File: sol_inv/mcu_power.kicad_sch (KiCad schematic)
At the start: 16 parts, among them SW1 SW_Push_Dual, U9 PSC3M5_E-LQFP-64

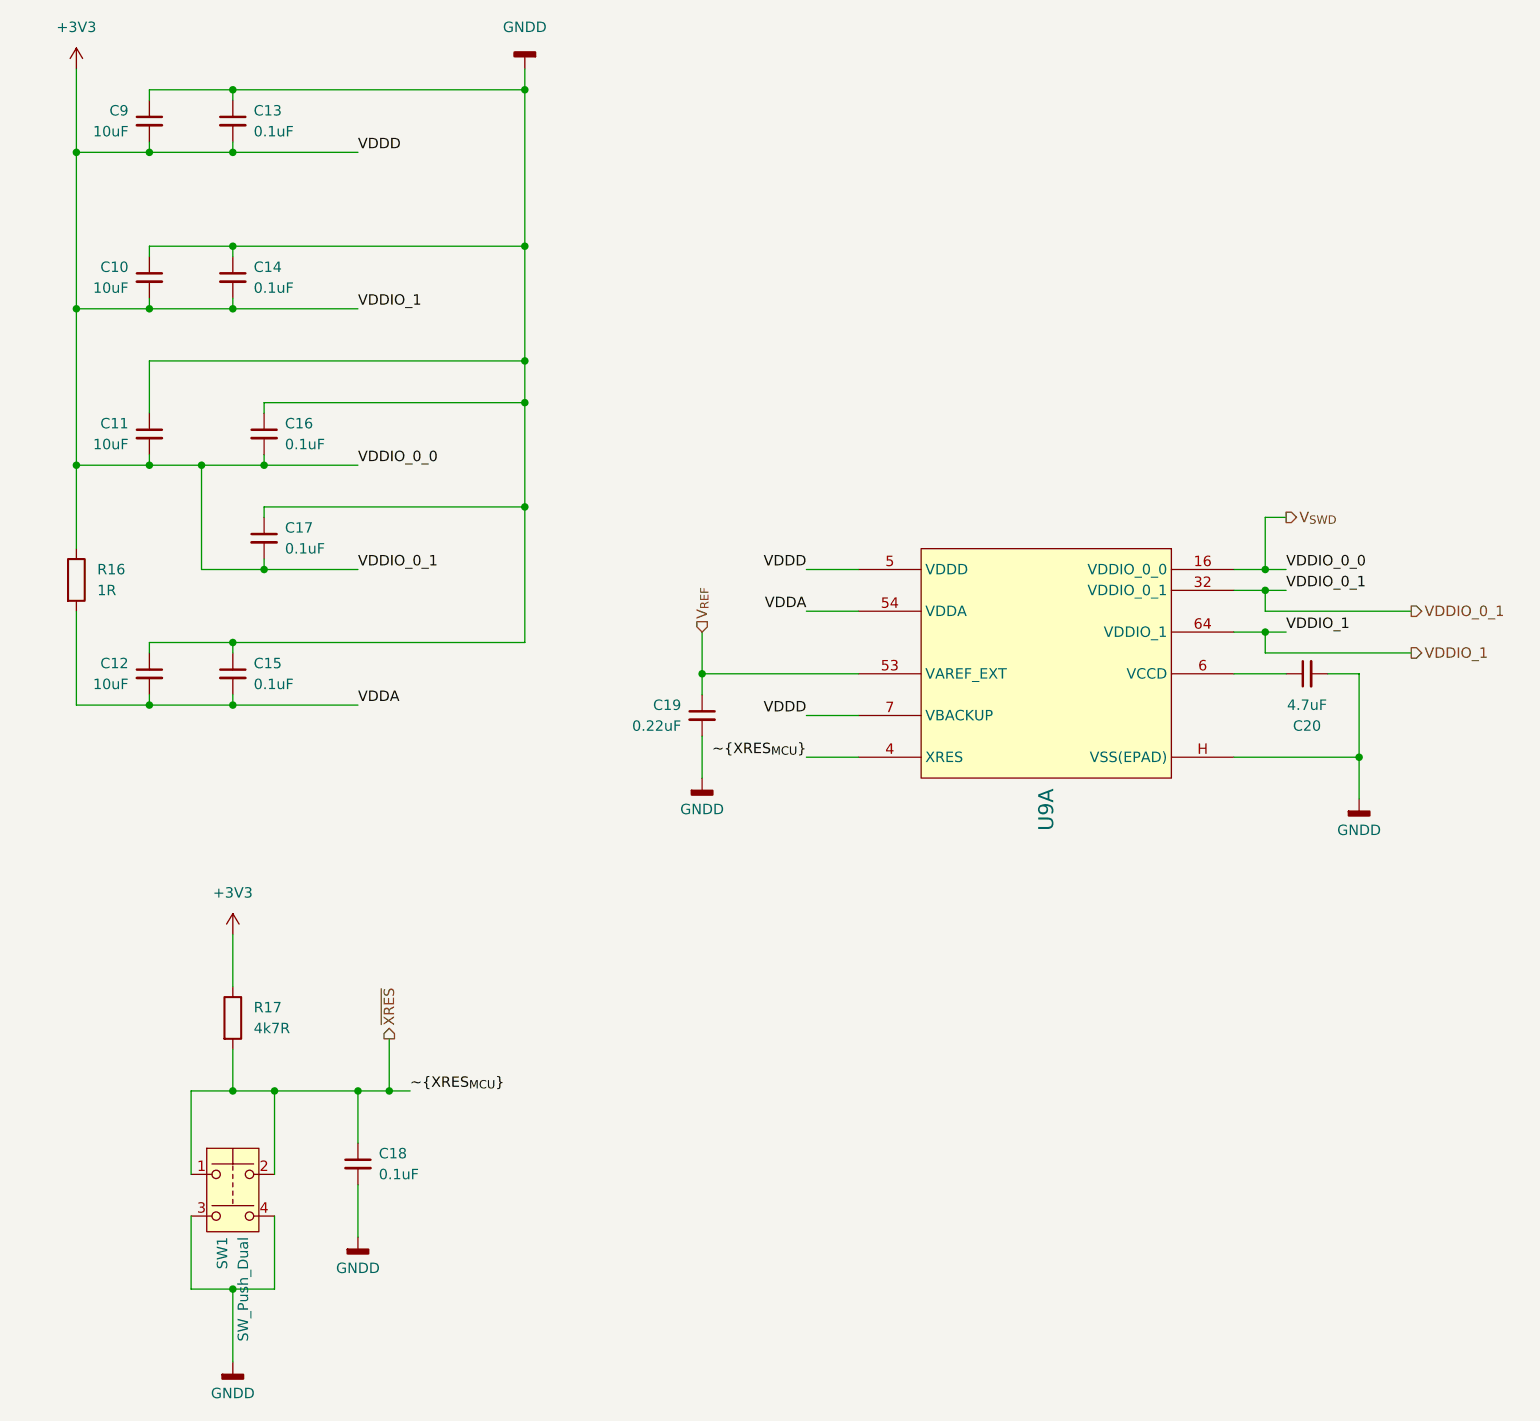
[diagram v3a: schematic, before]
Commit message: v0.3.4 fixes + component change for farnell
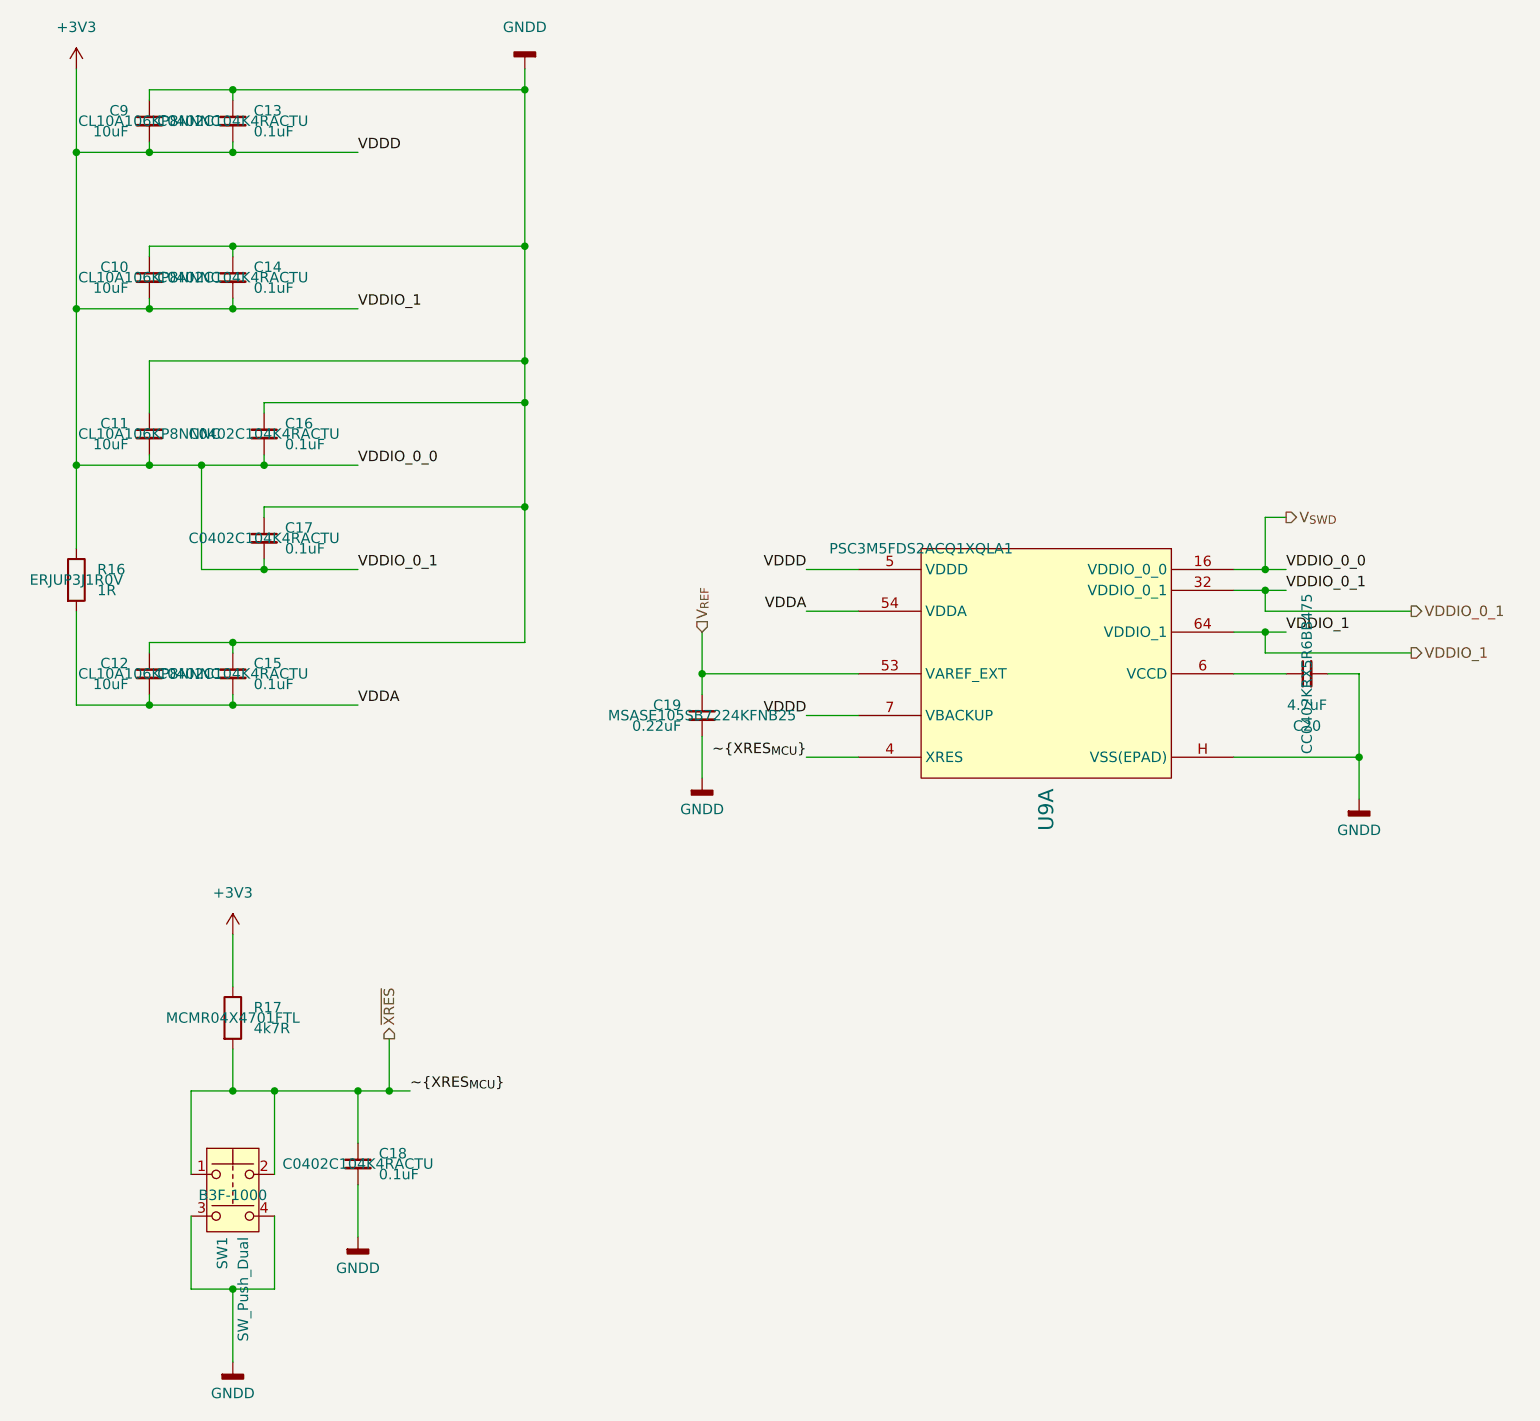
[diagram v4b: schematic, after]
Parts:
- C10, C11, C12, C9: Manufacturer Part Number (none) -> CL10A106KP8NNNC
- C13, C14, C15, C16, C17, C18: Manufacturer Part Number (none) -> C0402C104K4RACTU
- C19: Manufacturer Part Number (none) -> MSASE105SB7224KFNB25
- C20: Manufacturer Part Number (none) -> CC0402KRX5R6BB475
- R16: Manufacturer Part Number (none) -> ERJUP3J1R0V
- R17: Manufacturer Part Number (none) -> MCMR04X4701FTL
- SW1: Manufacturer Part Number (none) -> B3F-1000
- U9: Manufacturer Part Number (none) -> PSC3M5FDS2ACQ1XQLA1
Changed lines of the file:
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@@
+			)
+		)
+		(property "Manufacturer Part Number" "CC0402KRX5R6BB475"
+			(at 171.45 99.06 0)
+			(effects
+				(font
+					(size 1.27 1.27)
+				)
 			)
 		)
@@
 				)
 				(hide yes)
+			)
+		)
+		(property "Manufacturer Part Number" " B3F-1000"
+			(at 40.64 162.56 0)
+			(effects
+				(font
+					(size 1.27 1.27)
+				)
 			)
 		)
@@
 			)
 		)
+		(property "Manufacturer Part Number" "C0402C104K4RACTU"
+			(at 44.45 69.85 0)
+			(effects
+				(font
+					(size 1.27 1.27)
+				)
+			)
+		)
 		(pin "2"
 		)
@@
 			)
 		)
+		(property "Manufacturer Part Number" "MCMR04X4701FTL"
+			(at 40.64 140.97 0)
+			(effects
+				(font
+					(size 1.27 1.27)
+				)
+			)
+		)
 		(pin "2"
 		)
@@
 				)
 				(hide yes)
+			)
+		)
+		(property "Manufacturer Part Number" "MSASE105SB7224KFNB25"
+			(at 97.79 104.14 0)
+			(effects
+				(font
+					(size 1.27 1.27)
+				)
 			)
 		)
@@
 			)
 		)
+		(property "Manufacturer Part Number" "C0402C104K4RACTU"
+			(at 55.88 158.75 0)
+			(effects
+				(font
+					(size 1.27 1.27)
+				)
+			)
+		)
 		(pin "1"
 		)
@@
 				)
 				(hide yes)
+			)
+		)
+		(property "Manufacturer Part Number" "CL10A106KP8NNNC"
+			(at 30.48 69.85 0)
+			(effects
+				(font
+					(size 1.27 1.27)
+				)
 			)
 		)
@@
 			)
 		)
+		(property "Manufacturer Part Number" "C0402C104K4RACTU"
+			(at 40.64 31.75 0)
+			(effects
+				(font
+					(size 1.27 1.27)
+				)
+			)
+		)
 		(pin "2"
 		)
@@
 			)
 		)
+		(property "Manufacturer Part Number" "CL10A106KP8NNNC"
+			(at 30.48 99.06 0)
+			(effects
+				(font
+					(size 1.27 1.27)
+				)
+			)
+		)
 		(pin "2"
 		)
@@
 			)
 		)
+		(property "Manufacturer Part Number" "PSC3M5FDS2ACQ1XQLA1"
+			(at 124.46 83.82 0)
+			(effects
+				(font
+					(size 1.27 1.27)
+				)
+			)
+		)
 		(pin "58"
 		)
@@
 			)
 		)
+		(property "Manufacturer Part Number" "CL10A106KP8NNNC"
+			(at 30.48 50.8 0)
+			(effects
+				(font
+					(size 1.27 1.27)
+				)
+			)
+		)
 		(pin "2"
 		)
@@
 			)
 		)
+		(property "Manufacturer Part Number" "ERJUP3J1R0V"
+			(at 21.59 87.63 0)
+			(effects
+				(font
+					(size 1.27 1.27)
+				)
+			)
+		)
 		(pin "2"
 		)
@@
 			)
 		)
+		(property "Manufacturer Part Number" "C0402C104K4RACTU"
+			(at 40.64 99.06 0)
+			(effects
+				(font
+					(size 1.27 1.27)
+				)
+			)
+		)
 		(pin "2"
 		)
@@
 			)
 		)
+		(property "Manufacturer Part Number" "C0402C104K4RACTU"
+			(at 44.45 82.55 0)
+			(effects
+				(font
+					(size 1.27 1.27)
+				)
+			)
+		)
 		(pin "2"
 		)
@@
 				)
 				(hide yes)
+			)
+		)
+		(property "Manufacturer Part Number" "CL10A106KP8NNNC"
+			(at 30.48 31.75 0)
+			(effects
+				(font
+					(size 1.27 1.27)
+				)
 			)
 		)
@@
 			)
 		)
+		(property "Manufacturer Part Number" "C0402C104K4RACTU"
+			(at 40.64 50.8 0)
+			(effects
+				(font
+					(size 1.27 1.27)
+				)
+			)
+		)

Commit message: v0.4 fixed mcu ldo part, production testing
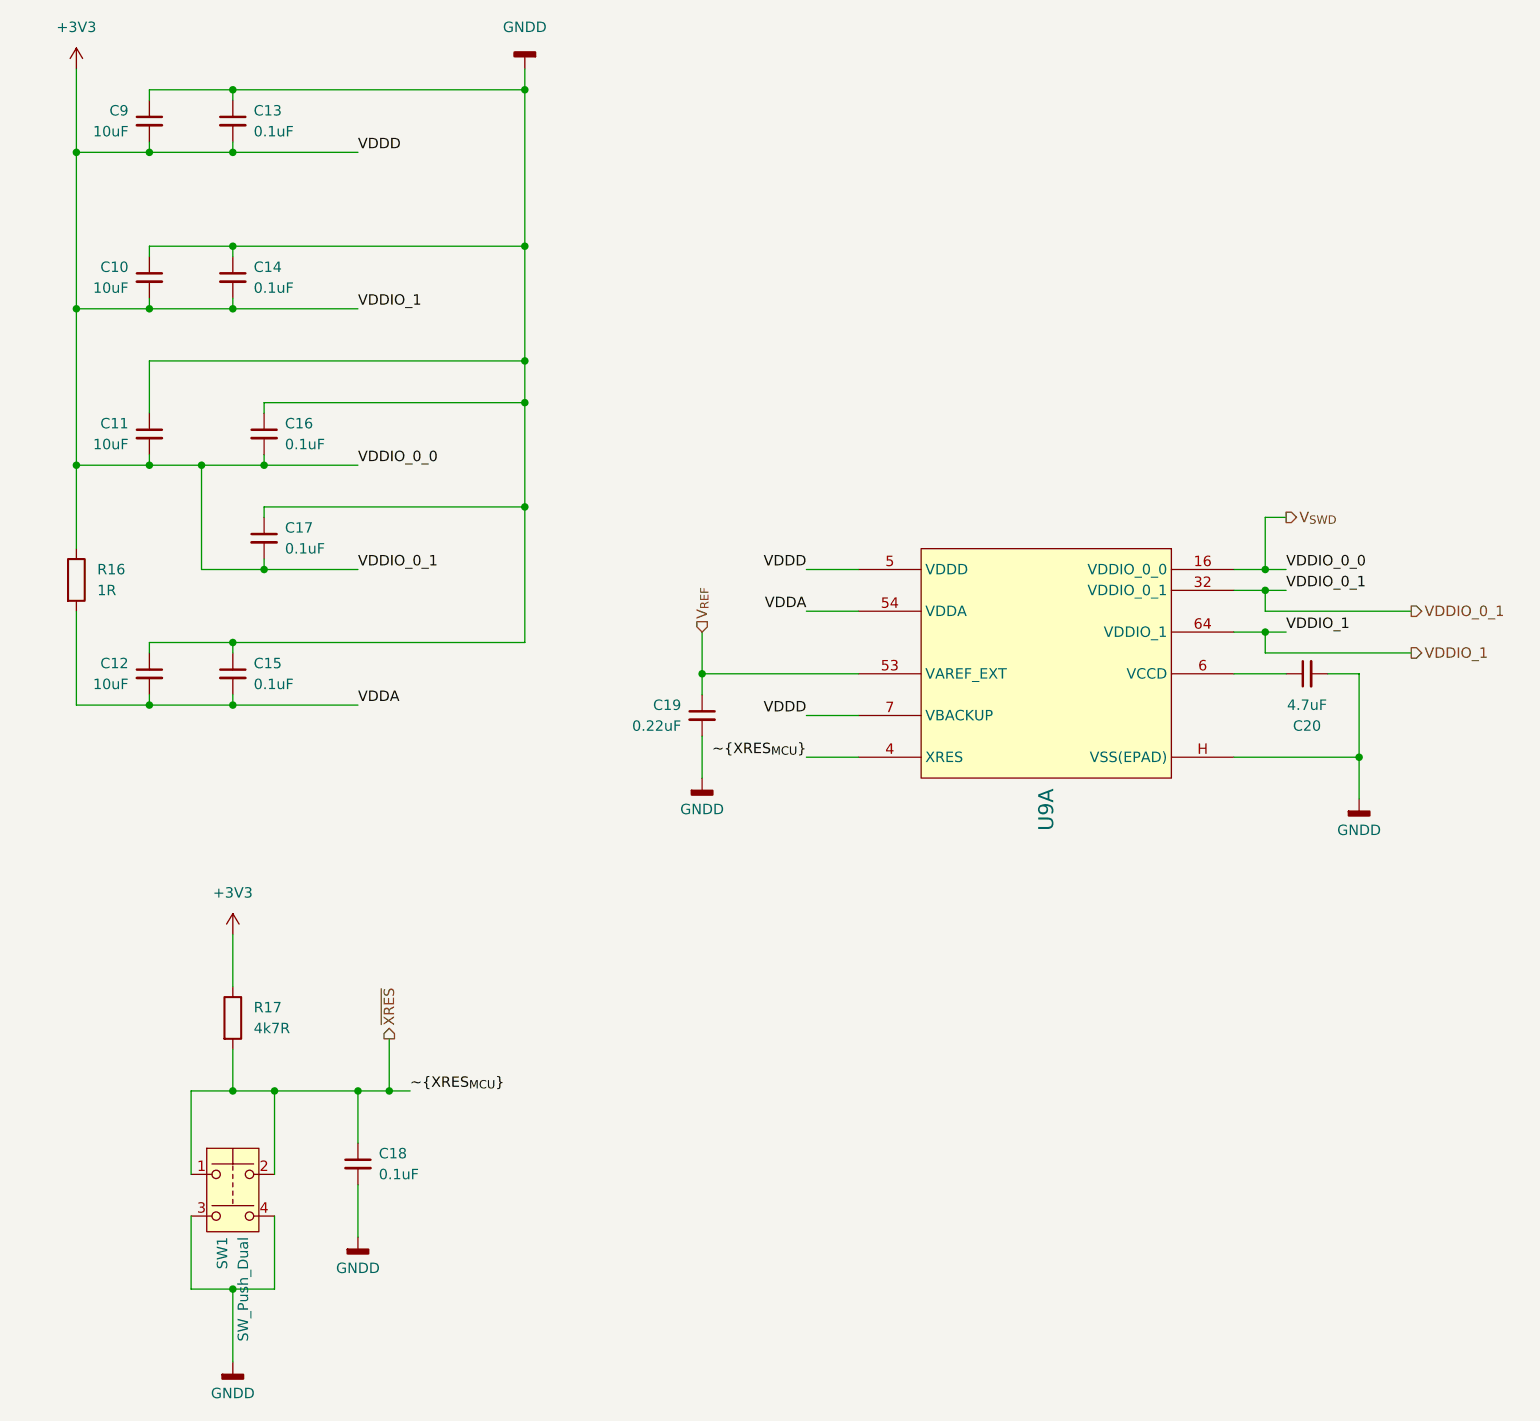
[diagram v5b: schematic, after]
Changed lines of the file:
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@@
 	(title_block
 		(title "MCU Power Delivery")
-		(date "2025-05-01")
-		(rev "0.3")
+		(date "2025-07-29")
+		(rev "0.4")
 		(company "Cezar-Octavian Bontaș")
 	)
@@
 					(size 1.27 1.27)
 				)
+				(hide yes)
+			)
+		)
+		(property "Sim.Enable" ""
+			(at 171.45 99.06 0)
+			(effects
+				(font
+					(size 1.27 1.27)
+				)
 			)
 		)
@@
 					(size 1.27 1.27)
 				)
+				(hide yes)
+			)
+		)
+		(property "Sim.Enable" ""
+			(at 40.64 162.56 0)
+			(effects
+				(font
+					(size 1.27 1.27)
+				)
 			)
 		)
@@
 					(size 1.27 1.27)
 				)
+				(hide yes)
+			)
+		)
+		(property "Sim.Enable" ""
+			(at 44.45 69.85 0)
+			(effects
+				(font
+					(size 1.27 1.27)
+				)
 			)
 		)
@@
 					(size 1.27 1.27)
 				)
+				(hide yes)
+			)
+		)
+		(property "Sim.Enable" ""
+			(at 40.64 140.97 0)
+			(effects
+				(font
+					(size 1.27 1.27)
+				)
 			)
 		)
@@
 					(size 1.27 1.27)
 				)
+				(hide yes)
+			)
+		)
+		(property "Sim.Enable" ""
+			(at 97.79 104.14 0)
+			(effects
+				(font
+					(size 1.27 1.27)
+				)
 			)
 		)
@@
 					(size 1.27 1.27)
 				)
+				(hide yes)
+			)
+		)
+		(property "Sim.Enable" ""
+			(at 55.88 158.75 0)
+			(effects
+				(font
+					(size 1.27 1.27)
+				)
 			)
 		)
@@
 					(size 1.27 1.27)
 				)
+				(hide yes)
+			)
+		)
+		(property "Sim.Enable" ""
+			(at 30.48 69.85 0)
+			(effects
+				(font
+					(size 1.27 1.27)
+				)
 			)
 		)
@@
 					(size 1.27 1.27)
 				)
+				(hide yes)
+			)
+		)
+		(property "Sim.Enable" ""
+			(at 40.64 31.75 0)
+			(effects
+				(font
+					(size 1.27 1.27)
+				)
 			)
 		)
@@
 					(size 1.27 1.27)
 				)
+				(hide yes)
+			)
+		)
+		(property "Sim.Enable" ""
+			(at 30.48 99.06 0)
+			(effects
+				(font
+					(size 1.27 1.27)
+				)
 			)
 		)
@@
 					(size 1.27 1.27)
 				)
+				(hide yes)
+			)
+		)
+		(property "Sim.Enable" ""
+			(at 124.46 83.82 0)
+			(effects
+				(font
+					(size 1.27 1.27)
+				)
 			)
 		)
@@
 					(size 1.27 1.27)
 				)
+				(hide yes)
+			)
+		)
+		(property "Sim.Enable" ""
+			(at 30.48 50.8 0)
+			(effects
+				(font
+					(size 1.27 1.27)
+				)
 			)
 		)
@@
 					(size 1.27 1.27)
 				)
+				(hide yes)
+			)
+		)
+		(property "Sim.Enable" ""
+			(at 21.59 87.63 0)
+			(effects
+				(font
+					(size 1.27 1.27)
+				)
 			)
 		)
@@
 					(size 1.27 1.27)
 				)
+				(hide yes)
+			)
+		)
+		(property "Sim.Enable" ""
+			(at 40.64 99.06 0)
+			(effects
+				(font
+					(size 1.27 1.27)
+				)
 			)
 		)
@@
 					(size 1.27 1.27)
 				)
+				(hide yes)
+			)
+		)
+		(property "Sim.Enable" ""
+			(at 44.45 82.55 0)
+			(effects
+				(font
+					(size 1.27 1.27)
+				)
 			)
 		)
@@
 					(size 1.27 1.27)
 				)
+				(hide yes)
+			)
+		)
+		(property "Sim.Enable" ""
+			(at 30.48 31.75 0)
+			(effects
+				(font
+					(size 1.27 1.27)
+				)
 			)
 		)
@@
 			(at 40.64 50.8 0)
 			(effects
+				(font
+					(size 1.27 1.27)
+				)
+				(hide yes)
+			)
+		)
+		(property "Sim.Enable" ""
+			(at 40.64 50.8 0)
+			(effects
